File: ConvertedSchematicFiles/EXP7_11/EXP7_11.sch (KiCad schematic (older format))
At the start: 12 parts, among them U1 uA741

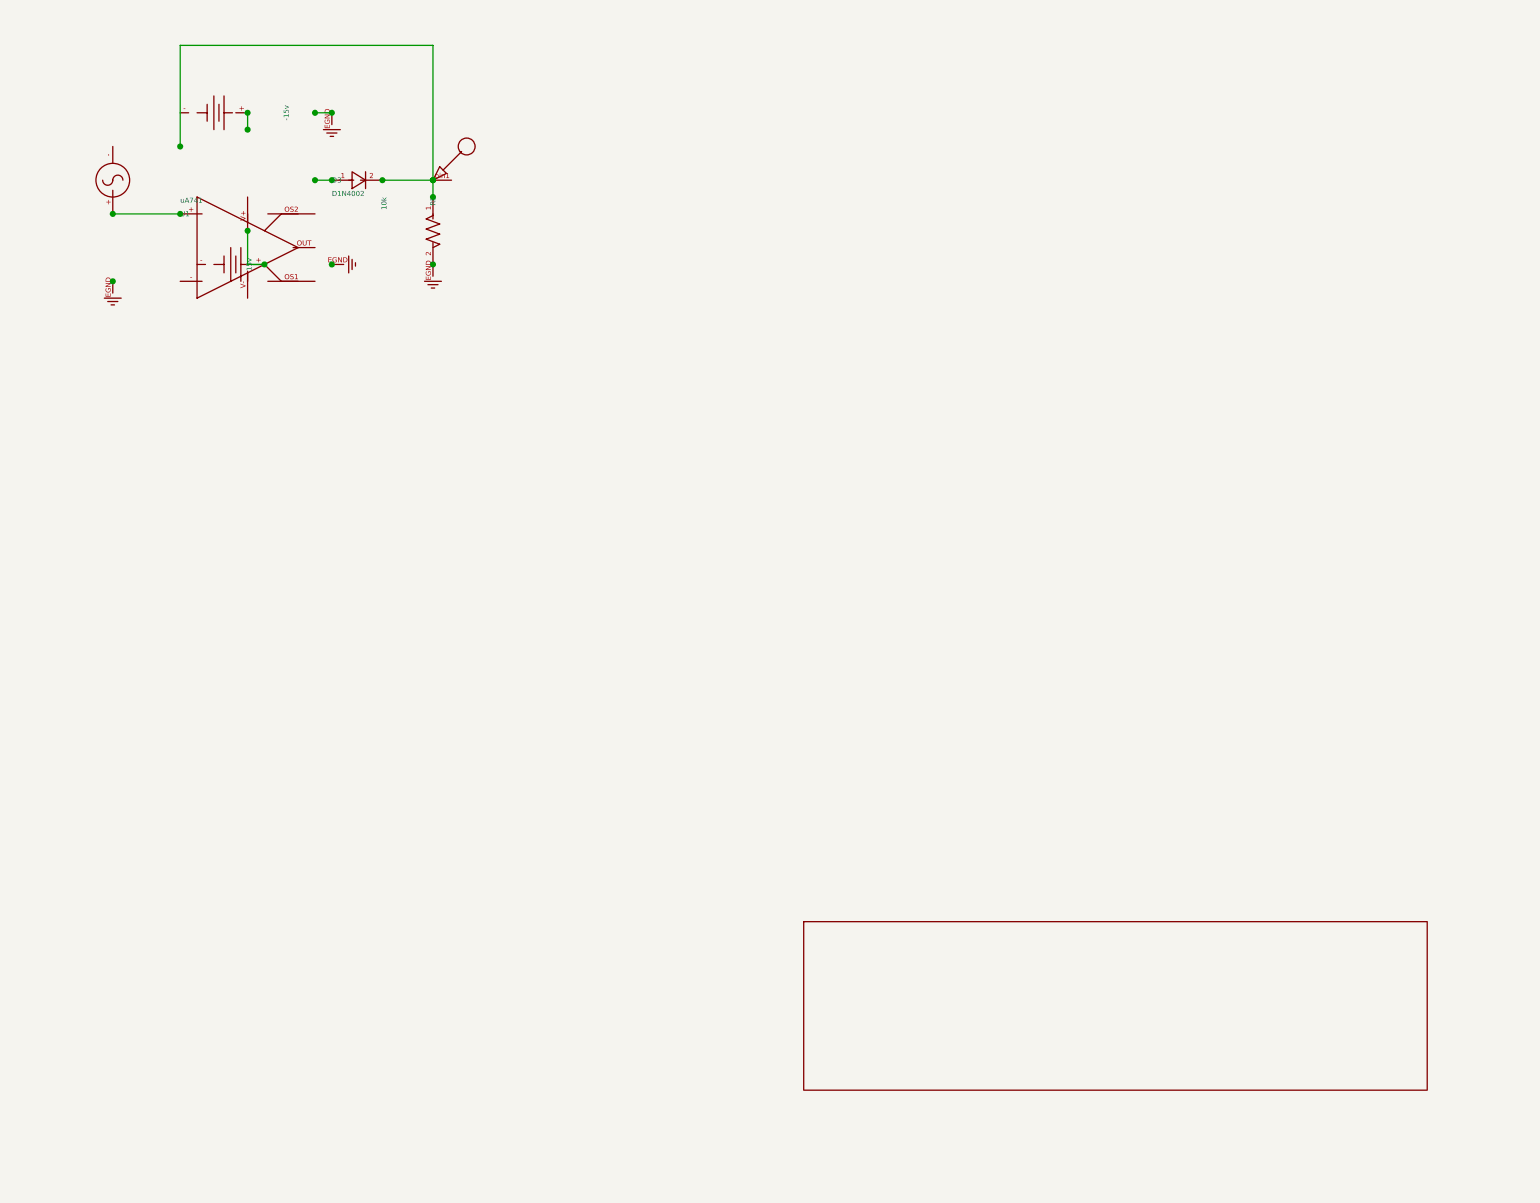
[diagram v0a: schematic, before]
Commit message: Excluded some components. These no longer appear after conversion. When calling shell commands, filenames are in "quotes"
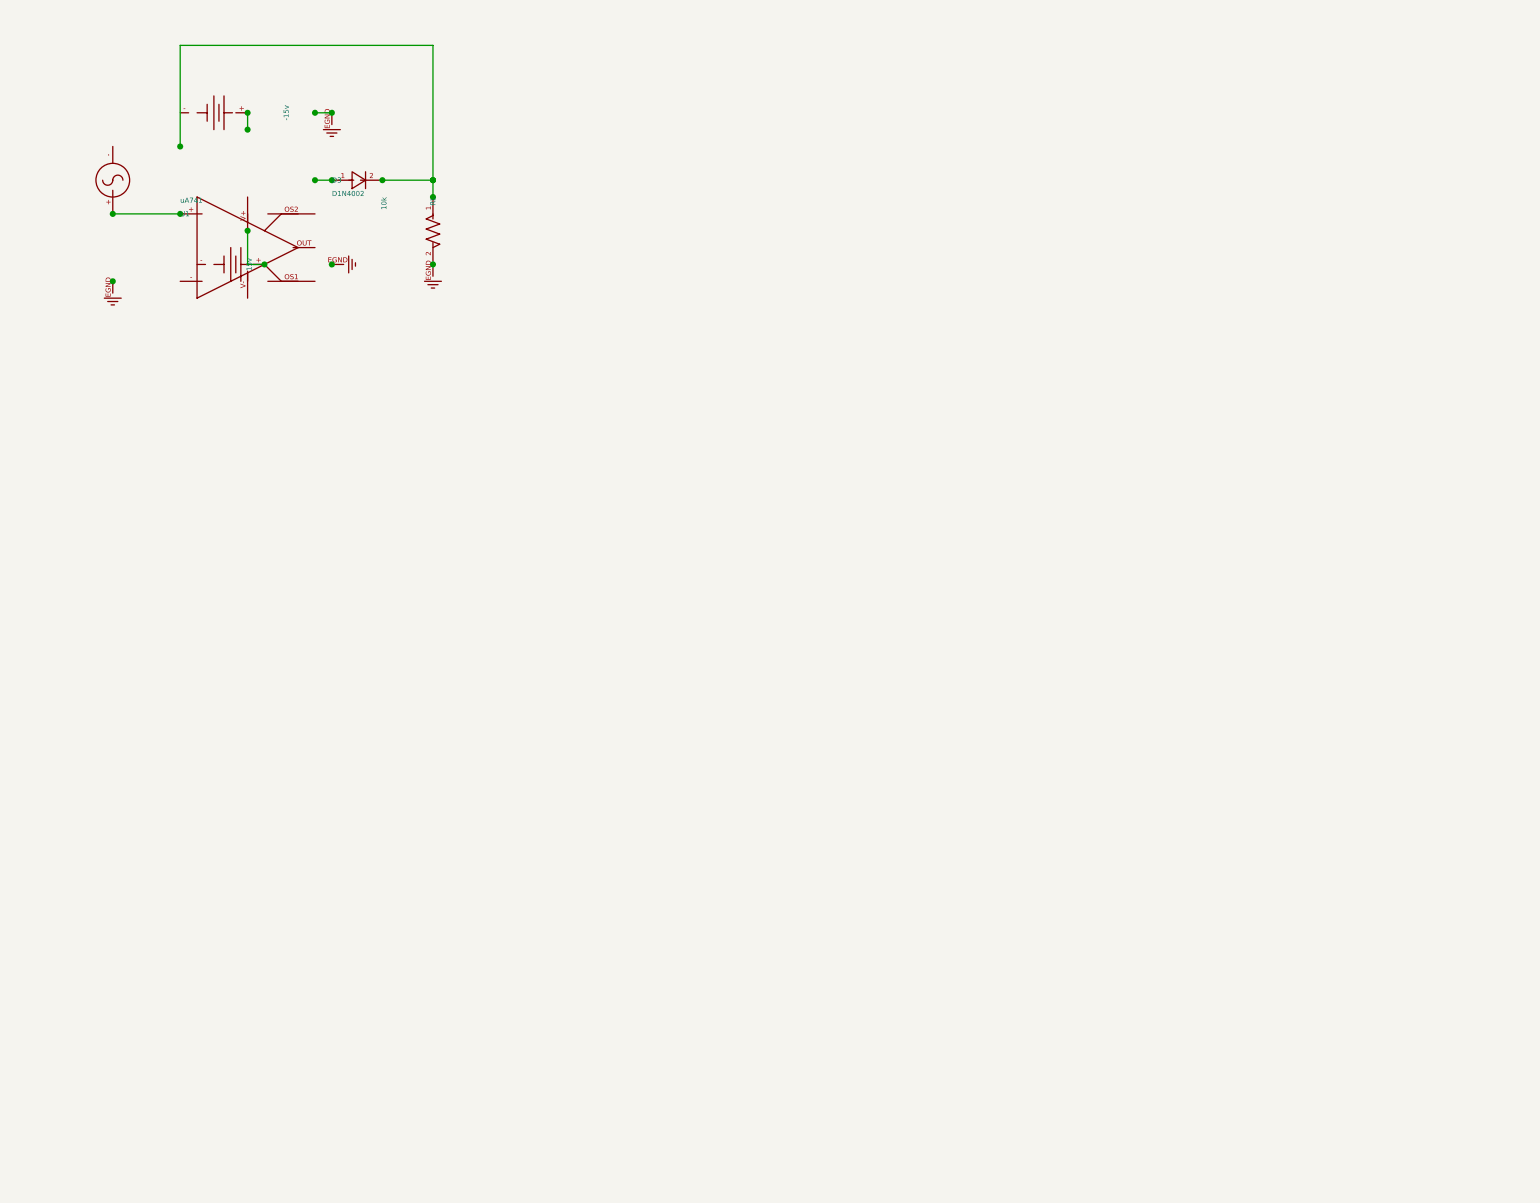
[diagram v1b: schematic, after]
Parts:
- removed nodeMarker: nodeMarker, symbol NODEMARKER_PSPICE
- removed titleblk: titleblk, symbol TITLEBLK_PSPICE
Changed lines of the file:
@@
-	1    0    0    1
-$EndComp
-$Comp
-L TITLEBLK_PSPICE titleblk
-U 1 1 45202362
-P 9700 7200
-F 0 "titleblk" H 19400 14400 30  0001 L CNN
-F 1 "titleblk" H 19400 14480 30  0001 L CNN
-	1    9700 7200
-	1    0    0    1
-$EndComp
-$Comp
-L NODEMARKER_PSPICE nodeMarker
-U 1 1 10490027
-P 3800 1800
-F 0 "nodeMarker" H 7600 3600 30  0001 L CNN
-F 1 "nodeMarker" H 7600 3680 30  0001 L CNN
-	1    3800 1800
 	1    0    0    1
 $EndComp

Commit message: Ports issue fixed. Now annotation for ports is #PWR? function added "itos"
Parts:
- removed EGND: EGND, symbol EGND_PSPICE
- removed GND_EARTH (x3): GND_EARTH, symbol GND_EARTH_PSPICE
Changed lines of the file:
@@
 $EndDescr
 $Comp
-L GND_EARTH_PSPICE GND_EARTH
+L GND_EARTH_PSPICE #PWR1
 U 1 1 14289383
 P 1900 2400
-F 0 "GND_EARTH" H 3800 4800 30  0001 L CNN
+F 0 "#PWR1" H 3800 4800 30  0001 L CNN
 F 1 "GND_EARTH" H 3800 4880 30  0001 L CNN
 	1    1900 2400
@@
 $EndComp
 $Comp
-L EGND_PSPICE EGND
+L EGND_PSPICE #PWR2
 U 1 1 46930886
 P 3800 2300
-F 0 "EGND" H 7600 4600 30  0001 L CNN
+F 0 "#PWR2" H 7600 4600 30  0001 L CNN
 F 1 "EGND" H 7600 4680 30  0001 L CNN
 	1    3800 2300
@@
 $EndComp
 $Comp
-L GND_EARTH_PSPICE GND_EARTH
+L GND_EARTH_PSPICE #PWR3
 U 1 1 71692777
 P 3200 2300
-F 0 "GND_EARTH" H 6400 4600 30  0001 L CNN
+F 0 "#PWR3" H 6400 4600 30  0001 L CNN
 F 1 "GND_EARTH" H 6400 4680 30  0001 L CNN
 	1    3200 2300
@@
 $EndComp
 $Comp
-L GND_EARTH_PSPICE GND_EARTH
+L GND_EARTH_PSPICE #PWR4
 U 1 1 14636915
 P 3200 1400
-F 0 "GND_EARTH" H 6400 2800 30  0001 L CNN
+F 0 "#PWR4" H 6400 2800 30  0001 L CNN
 F 1 "GND_EARTH" H 6400 2880 30  0001 L CNN
 	1    3200 1400

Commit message: Added LICENSE.txt
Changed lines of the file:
@@
 $EndDescr
 $Comp
-L GND_EARTH_PSPICE #PWR1
+L GND #PWR1
 U 1 1 14289383
 P 1900 2400
@@
 $EndComp
 $Comp
-L EGND_PSPICE #PWR2
+L GND #PWR2
 U 1 1 46930886
 P 3800 2300
@@
 $EndComp
 $Comp
-L GND_EARTH_PSPICE #PWR3
+L GND #PWR3
 U 1 1 71692777
 P 3200 2300
@@
 $EndComp
 $Comp
-L GND_EARTH_PSPICE #PWR4
+L GND #PWR4
 U 1 1 14636915
 P 3200 1400

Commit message: Orientation fix. Library components are now inverted, with +ve y axis going up. In Schematic files, +ve y axis is downwards. This is how the KiCad libraries are. As a result of the above fixed, the converted GND is now oriented correctly.
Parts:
- VIN: value VSIN -> SINE
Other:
- moved on the sheet: U1
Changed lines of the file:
@@
 F 1 "GND_EARTH" H 3800 4880 30  0001 L CNN
 	1    1900 2400
-	1    0    0    1
+	1    0    0    -1
 $EndComp
 $Comp
@@
 F 1 "EGND" H 7600 4680 30  0001 L CNN
 	1    3800 2300
-	1    0    0    1
+	1    0    0    -1
 $EndComp
 $Comp
@@
 F 1 "GND_EARTH" H 6400 4680 30  0001 L CNN
 	1    3200 2300
-	0    1    -1    0
+	0    -1    -1    0
 $EndComp
 $Comp
@@
 F 1 "GND_EARTH" H 6400 2880 30  0001 L CNN
 	1    3200 1400
-	1    0    0    1
+	1    0    0    -1
 $EndComp
 $Comp
@@
 F 1 "10k" H 3800 2190 30  0000 L CNN
 	1    3800 1900
-	0    -1    1    0
+	0    1    1    0
 $EndComp
 $Comp
@@
 F 1 "15v" H 2800 2210 30  0000 C CNN
 	1    2800 2300
-	0    1    -1    0
+	0    -1    -1    0
 $EndComp
 $Comp
@@
 P 1900 2000
 F 0 "VIN" H 1900 2000 30  0001 L CNN
-F 1 "VSIN" H 1900 2080 30  0001 L CNN
+F 1 "SINE" H 1900 2080 30  0001 L CNN
 	1    1900 2000
-	1    0    0    1
+	1    0    0    -1
 $EndComp
 $Comp
@@
 F 1 "-15v" H 2700 1630 30  0000 C CNN
 	1    2700 1400
-	0    1    -1    0
+	0    -1    -1    0
 $EndComp
 $Comp
@@
 F 1 "uA741" H 2300 2080 30  0000 L CNN
 	1    2300 2000
-	1    0    0    -1
+	1    0    0    1
 $EndComp
 $Comp
@@
 F 1 "D1N4002" H 3200 1880 30  0000 L CNN
 	1    3200 1800
-	1    0    0    1
+	1    0    0    -1
 $EndComp
 Wire Wire Line

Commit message: Removed the use of exec, wrote basename function, made integration with eSim easier.
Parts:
- added nodeMarker: nodeMarker, symbol nodeMarker_PSPICE
- added titleblk: titleblk, symbol titleblk_PSPICE
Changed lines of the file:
@@
-EESchema Schematic File Version 2  date Tuesday 22 June 1999 12:24:08 AM IST
+EESchema Schematic File Version 2  date
 LIBS:power
 LIBS:device
@@
 LIBS:contrib
 LIBS:valves
-LIBS:ConvertedSchematicFiles/EXP7_11-cache
 EELAYER 25  0
 EELAYER END
@@
 Sheet 1 1
 Title ""
-Date "22 Jun 1999"
+Date ""
 Rev ""
 Comp ""
@@
 	1    0    0    -1
 $EndComp
+$Comp
+L titleblk_PSPICE titleblk
+U 1 1 45202362
+P 9700 7200
+F 0 "titleblk" H 19400 14400 30  0001 L CNN
+F 1 "titleblk" H 19400 14480 30  0001 L CNN
+	1    9700 7200
+	1    0    0    -1
+$EndComp
+$Comp
+L nodeMarker_PSPICE nodeMarker
+U 1 1 10490027
+P 3800 1800
+F 0 "nodeMarker" H 7600 3600 30  0001 L CNN
+F 1 "nodeMarker" H 7600 3680 30  0001 L CNN
+	1    3800 1800
+	1    0    0    -1
+$EndComp
